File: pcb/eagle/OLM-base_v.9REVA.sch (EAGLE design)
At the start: 34 parts, among them IC1 ATMEGA, IC2 MCP1702-33, IC3 ENC28J60SP, J1 POWER_JACKPTH, J2 MAGJACK, X1 16 MHz, X2 25MHz

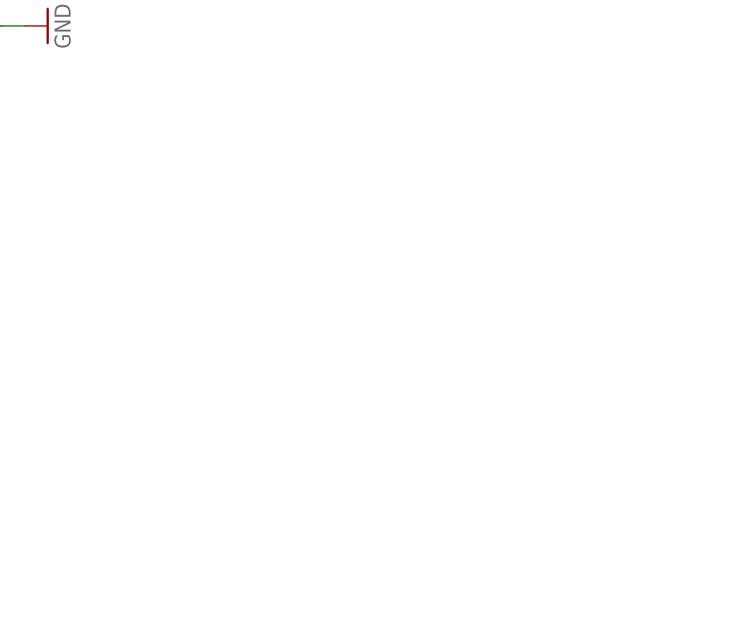
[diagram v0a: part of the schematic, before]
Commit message: added RTC
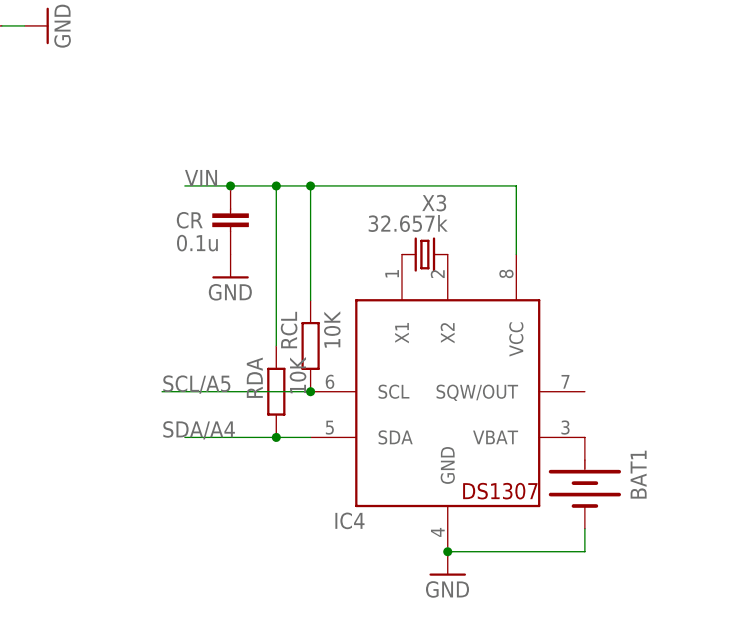
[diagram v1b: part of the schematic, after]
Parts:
- added BAT1: (no value), SparkFun:BATTERY12PTH
- added CR: 0.1u, rcl:C-EU025-024X044
- added IC4: DS1307, adafruit:DS1307
- added RCL, RDA: 10K, rcl:R-EU_0204/7
- added X3: 32.657k, crystal:CRYSTALTC26H
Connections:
- new net N$36: BAT1.+, IC4.VBAT
- new net N$47: IC4.X2, X3.2
- new net N$57: IC4.X1, X3.1
- net GND: now also BAT1.-, CR.2, IC4.GND
- net SCL/A5: now also IC4.SCL, RCL.2
- net SDA/A4: now also IC4.SDA, RDA.2
- net VIN: now also CR.1, IC4.VCC, RCL.1, RDA.1
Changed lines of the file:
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@@
 <part name="J1" library="SparkFun-Connectors" deviceset="POWER_JACK" device="PTH"/>
 <part name="JP2" library="pinhead" deviceset="PINHD-2X5" device=""/>
+<part name="GND6" library="SparkFun" deviceset="GND" device=""/>
+<part name="BAT1" library="SparkFun" deviceset="BATTERY" device="12PTH"/>
+<part name="IC4" library="adafruit" deviceset="DS1307" device=""/>
+<part name="RCL" library="rcl" deviceset="R-EU_" device="0204/7" value="10K"/>
+<part name="RDA" library="rcl" deviceset="R-EU_" device="0204/7" value="10K"/>
+<part name="X3" library="crystal" deviceset="CRYSTAL" device="TC26H" value="32.657k"/>
+<part name="CR" library="rcl" deviceset="C-EU" device="025-024X044" value="0.1u"/>
+<part name="GND10" library="SparkFun" deviceset="GND" device=""/>
 </parts>
 <sheets>
@@
 <instance part="J1" gate="G$1" x="-12.7" y="-68.58"/>
 <instance part="JP2" gate="A" x="62.23" y="-78.74"/>
+<instance part="GND6" gate="1" x="191.77" y="-114.3"/>
+<instance part="BAT1" gate="G$1" x="207.01" y="-104.14" rot="R270"/>
+<instance part="IC4" gate="G$1" x="191.77" y="-96.52"/>
+<instance part="RCL" gate="G$1" x="176.53" y="-88.9" rot="MR270"/>
+<instance part="RDA" gate="G$1" x="172.72" y="-93.98" rot="MR270"/>
+<instance part="X3" gate="G$1" x="189.23" y="-78.74" smashed="yes" rot="MR180">
+<attribute name="NAME" x="191.77" y="-73.914" size="1.778" layer="95" rot="MR0"/>
+<attribute name="VALUE" x="191.77" y="-76.2" size="1.778" layer="96" rot="MR0"/>
+</instance>
+<instance part="CR" gate="G$1" x="167.64" y="-73.66" smashed="yes">
+<attribute name="NAME" x="161.544" y="-75.819" size="1.778" layer="95"/>
+<attribute name="VALUE" x="161.544" y="-78.359" size="1.778" layer="96"/>
+</instance>
+<instance part="GND10" gate="1" x="167.64" y="-81.28"/>
 </instances>
 <busses>
@@
 <wire x1="59.69" y1="-76.2" x2="43.18" y2="-76.2" width="0.1524" layer="91"/>
 </segment>
+<segment>
+<wire x1="191.77" y1="-111.76" x2="207.01" y2="-111.76" width="0.1524" layer="91"/>
+<wire x1="207.01" y1="-111.76" x2="207.01" y2="-109.22" width="0.1524" layer="91"/>
+<junction x="191.77" y="-111.76"/>
+<pinref part="IC4" gate="G$1" pin="GND"/>
+<pinref part="GND6" gate="1" pin="GND"/>
+<pinref part="BAT1" gate="G$1" pin="-"/>
+</segment>
+<segment>
+<pinref part="CR" gate="G$1" pin="2"/>
+<pinref part="GND10" gate="1" pin="GND"/>
+</segment>
 </net>
 <net name="N$19" class="0">
@@
 <wire x1="67.31" y1="-81.28" x2="78.74" y2="-81.28" width="0.1524" layer="91"/>
 </segment>
+<segment>
+<wire x1="172.72" y1="-88.9" x2="172.72" y2="-71.12" width="0.1524" layer="91"/>
+<wire x1="199.39" y1="-78.74" x2="199.39" y2="-71.12" width="0.1524" layer="91"/>
+<wire x1="199.39" y1="-71.12" x2="176.53" y2="-71.12" width="0.1524" layer="91"/>
+<wire x1="176.53" y1="-71.12" x2="172.72" y2="-71.12" width="0.1524" layer="91"/>
+<wire x1="172.72" y1="-71.12" x2="167.64" y2="-71.12" width="0.1524" layer="91"/>
+<wire x1="167.64" y1="-71.12" x2="162.56" y2="-71.12" width="0.1524" layer="91"/>
+<wire x1="176.53" y1="-83.82" x2="176.53" y2="-71.12" width="0.1524" layer="91"/>
+<junction x="172.72" y="-71.12"/>
+<junction x="176.53" y="-71.12"/>
+<junction x="167.64" y="-71.12"/>
+<label x="162.56" y="-71.12" size="1.778" layer="95"/>
+<pinref part="RDA" gate="G$1" pin="1"/>
+<pinref part="IC4" gate="G$1" pin="VCC"/>
+<pinref part="RCL" gate="G$1" pin="1"/>
+<pinref part="CR" gate="G$1" pin="1"/>
+</segment>
 </net>
 <net name="D3/PWM" class="0">
@@
 <wire x1="59.69" y1="-83.82" x2="43.18" y2="-83.82" width="0.1524" layer="91"/>
 </segment>
+<segment>
+<wire x1="176.53" y1="-99.06" x2="172.72" y2="-99.06" width="0.1524" layer="91"/>
+<wire x1="172.72" y1="-99.06" x2="162.56" y2="-99.06" width="0.1524" layer="91"/>
+<junction x="172.72" y="-99.06"/>
+<label x="160.02" y="-99.06" size="1.778" layer="95"/>
+<pinref part="IC4" gate="G$1" pin="SDA"/>
+<pinref part="RDA" gate="G$1" pin="2"/>
+</segment>
 </net>
 <net name="SCL/A5" class="0">
@@
 <pinref part="JP2" gate="A" pin="7"/>
 <wire x1="59.69" y1="-81.28" x2="43.18" y2="-81.28" width="0.1524" layer="91"/>
+</segment>
+<segment>
+<wire x1="176.53" y1="-93.98" x2="160.02" y2="-93.98" width="0.1524" layer="91"/>
+<junction x="176.53" y="-93.98"/>
+<label x="160.02" y="-93.98" size="1.778" layer="95"/>
+<pinref part="IC4" gate="G$1" pin="SCL"/>
+<pinref part="RCL" gate="G$1" pin="2"/>
 </segment>
 </net>
@@
 </segment>
 </net>
+<net name="N$36" class="0">
+<segment>
+<pinref part="IC4" gate="G$1" pin="VBAT"/>
+<pinref part="BAT1" gate="G$1" pin="+"/>
+</segment>
+</net>
+<net name="N$47" class="0">
+<segment>
+<pinref part="IC4" gate="G$1" pin="X2"/>
+<pinref part="X3" gate="G$1" pin="2"/>
+</segment>
+</net>
+<net name="N$57" class="0">
+<segment>
+<pinref part="IC4" gate="G$1" pin="X1"/>
+<pinref part="X3" gate="G$1" pin="1"/>
+</segment>
+</net>
